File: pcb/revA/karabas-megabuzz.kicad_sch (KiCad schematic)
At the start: 1 part

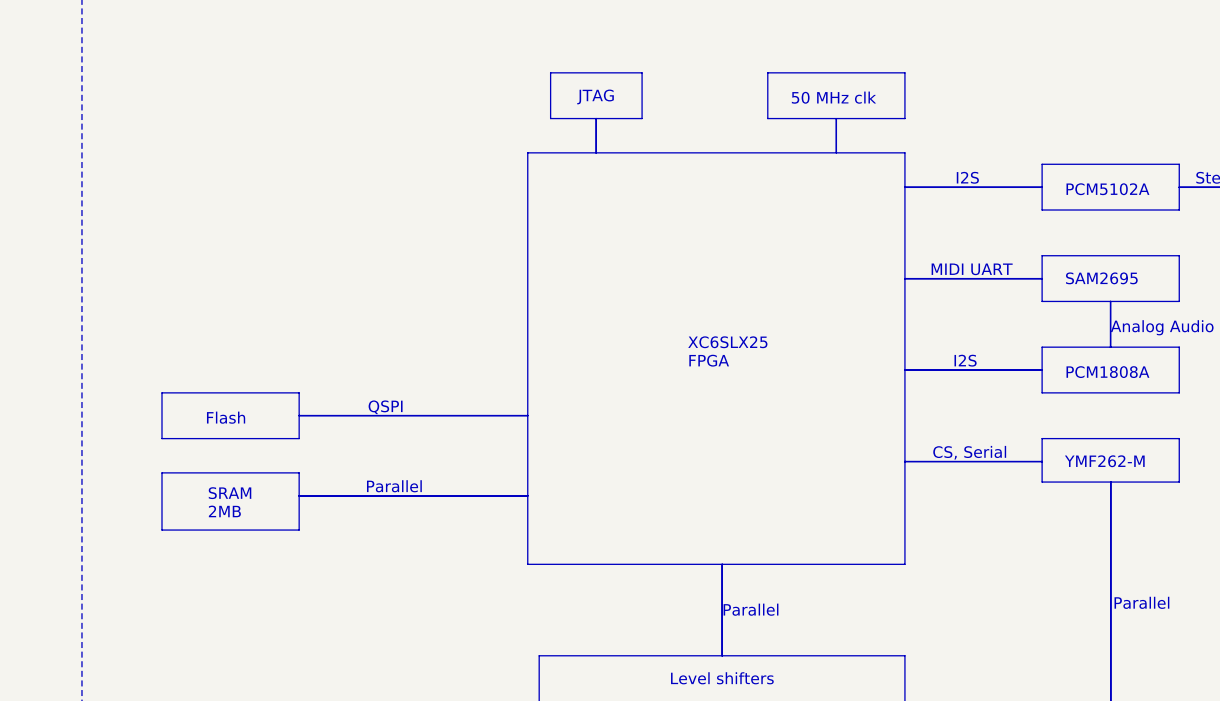
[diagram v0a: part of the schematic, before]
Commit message: Updated gerbers to min 0.2/0.45 vias, firmware build for xc6slx16
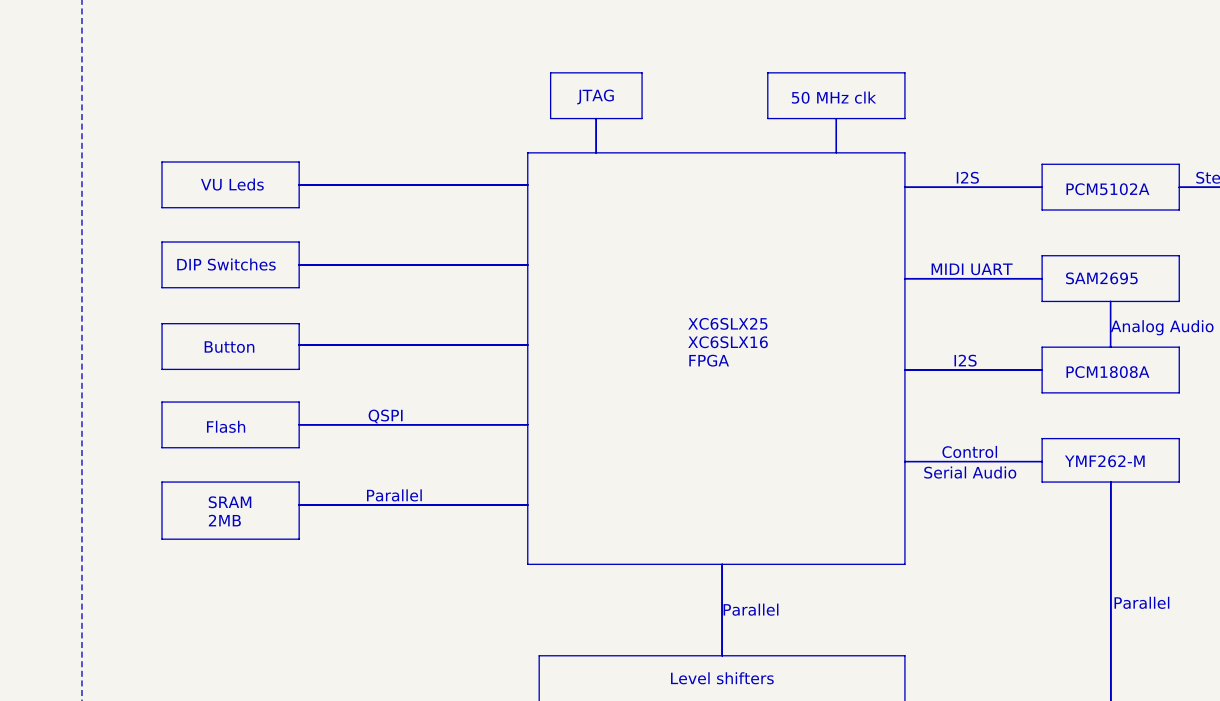
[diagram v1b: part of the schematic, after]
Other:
- note added: "Button"
- note added: "Control"
- note added: "DIP Switches"
- note added: "Serial Audio"
- note added: "VU Leds"
- note added: "XC6SLX25 XC6SLX16 FPGA"
- note removed: "CS, Serial"
- note removed: "XC6SLX25 FPGA"
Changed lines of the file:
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@@
+	)
+	(rectangle
+		(start 124.46 82.55)
+		(end 149.86 82.5754)
+		(stroke
+			(width 0)
+			(type default)
+		)
+		(fill
+			(type none)
+		)
+	)
+	(rectangle
+		(start 124.46 73.66)
+		(end 149.86 73.6854)
+		(stroke
+			(width 0)
+			(type default)
+		)
+		(fill
+			(type none)
+		)
 	)
 	(rectangle
@@
 	)
 	(rectangle
-		(start 109.22 105.664)
-		(end 124.46 112.014)
+		(start 109.22 106.68)
+		(end 124.46 113.03)
 		(stroke
 			(width 0)
@@
 	)
 	(rectangle
+		(start 124.46 91.44)
+		(end 149.86 91.4654)
+		(stroke
+			(width 0)
+			(type default)
+		)
+		(fill
+			(type none)
+		)
+	)
+	(rectangle
 		(start 214.6046 86.614)
 		(end 214.63 91.694)
@@
 	)
 	(rectangle
-		(start 124.46 99.2886)
-		(end 149.86 99.314)
-		(stroke
-			(width 0)
-			(type default)
-		)
-		(fill
-			(type none)
-		)
-	)
-	(rectangle
-		(start 109.22 96.774)
-		(end 124.46 101.854)
+		(start 124.46 100.3046)
+		(end 149.86 100.33)
+		(stroke
+			(width 0)
+			(type default)
+		)
+		(fill
+			(type none)
+		)
+	)
+	(rectangle
+		(start 109.22 97.79)
+		(end 124.46 102.87)
 		(stroke
 			(width 0)
@@
 	)
 	(rectangle
+		(start 109.2236 89.0839)
+		(end 124.4636 94.1639)
+		(stroke
+			(width 0)
+			(type default)
+		)
+		(fill
+			(type color)
+			(color 255 255 194 1)
+		)
+	)
+	(rectangle
+		(start 109.22 80.01)
+		(end 124.46 85.09)
+		(stroke
+			(width 0)
+			(type default)
+		)
+		(fill
+			(type color)
+			(color 255 255 194 1)
+		)
+	)
+	(rectangle
 		(start 191.77 104.394)
 		(end 207.01 104.4194)
@@
 	)
 	(rectangle
+		(start 109.22 71.12)
+		(end 124.46 76.2)
+		(stroke
+			(width 0)
+			(type default)
+		)
+		(fill
+			(type color)
+			(color 255 255 194 1)
+		)
+	)
+	(rectangle
 		(start 191.77 137.16)
 		(end 214.63 137.1854)
@@
 	)
 	(rectangle
-		(start 124.46 108.204)
-		(end 149.86 108.2294)
+		(start 124.46 109.22)
+		(end 149.86 109.2454)
 		(stroke
 			(width 0)
@@
 		)
 	)
-	(text "XC6SLX25\nFPGA"
+	(text "VU Leds"
+		(exclude_from_sim no)
+		(at 113.538 74.676 0)
+		(effects
+			(font
+				(size 1.27 1.27)
+			)
+			(justify left bottom)
+		)
+	)
+	(text "XC6SLX25\nXC6SLX16\nFPGA"
 		(exclude_from_sim no)
 		(at 167.64 94.234 0)
@@
 		)
 	)
+	(text "Button"
+		(exclude_from_sim no)
+		(at 113.792 92.71 0)
+		(effects
+			(font
+				(size 1.27 1.27)
+			)
+			(justify left bottom)
+		)
+	)
 	(text "PCM1808A"
 		(exclude_from_sim no)
@@
 	(text "Parallel"
 		(exclude_from_sim no)
-		(at 131.826 108.204 0)
+		(at 131.826 109.22 0)
 		(effects
 			(font
@@
 		)
 	)
+	(text "DIP Switches"
+		(exclude_from_sim no)
+		(at 110.744 83.566 0)
+		(effects
+			(font
+				(size 1.27 1.27)
+			)
+			(justify left bottom)
+		)
+	)
 	(text "Audio Out"
 		(exclude_from_sim no)
@@
 	(text "QSPI"
 		(exclude_from_sim no)
-		(at 132.08 99.314 0)
+		(at 132.08 100.33 0)
 		(effects
 			(font
@@
 	(text "Flash"
 		(exclude_from_sim no)
-		(at 114.046 100.584 0)
+		(at 114.046 101.6 0)
 		(effects
 			(font
@@
 	(text "SRAM\n2MB"
 		(exclude_from_sim no)
-		(at 114.3 110.998 0)
+		(at 114.3 112.014 0)
 		(effects
 			(font
@@
 		)
 	)
-	(text "CS, Serial"
-		(exclude_from_sim no)
-		(at 194.818 104.394 0)
+	(text "Control"
+		(exclude_from_sim no)
+		(at 195.834 104.394 0)
+		(effects
+			(font
+				(size 1.27 1.27)
+			)
+			(justify left bottom)
+		)
+	)
+	(text "Serial Audio"
+		(exclude_from_sim no)
+		(at 193.802 106.68 0)
 		(effects
 			(font
@@
 			(effects
 				(font
-					(size 1 1)
+					(size 0.9906 0.9906)
 				)
 			)
@@
 			(effects
 				(font
-					(size 1 1)
+					(size 0.9906 0.9906)
 				)
 			)
